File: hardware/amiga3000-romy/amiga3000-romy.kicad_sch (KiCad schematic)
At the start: 5 parts, among them IC1 GAL22V10, IC2 FAT_GARY

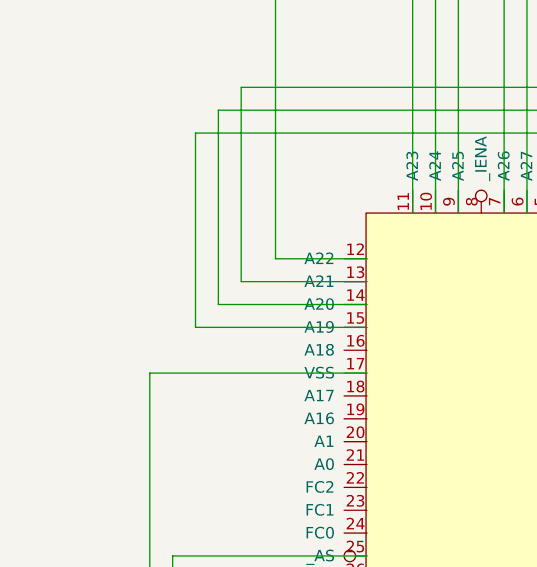
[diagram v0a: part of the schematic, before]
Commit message: Update Amiga3000 ROMY to Rev4a
major difference is the address header to support 4MB ROMs
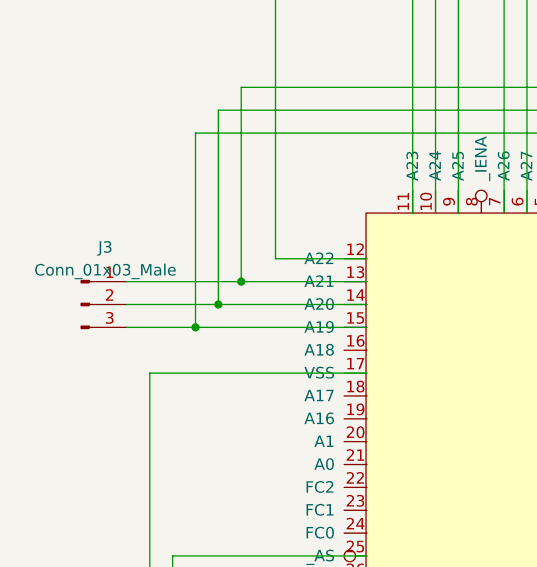
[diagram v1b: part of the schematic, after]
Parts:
- added J3: Conn_01x03_Male, Connector_PinHeader_2.54mm:PinHeader_1x03_P2.54mm_Horizontal, symbol Connector:Conn_01x03_Male
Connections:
- net at IC1.25 (IO3), IC2.13 (A21): now also J3.1 (Pin_1)
- net at IC1.24 (IO4), IC2.14 (A20): now also J3.2 (Pin_2)
- net at IC1.23 (IO5), IC2.15 (A19): now also J3.3 (Pin_3)
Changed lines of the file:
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@@
-(kicad_sch (version 20210126) (generator eeschema)
+(kicad_sch (version 20210406) (generator eeschema)
   (paper "A4")
   (title_block
@@
     (comment 4 "Re-implementation of A4k ROMY")
   )
+  (junction (at 41.91 88.9) (diameter 0.9144) (color 0 0 0 0))
+  (junction (at 44.45 86.36) (diameter 0.9144) (color 0 0 0 0))
+  (junction (at 46.99 83.82) (diameter 0.9144) (color 0 0 0 0))
   (junction (at 68.58 148.59) (diameter 0.9144) (color 0 0 0 0))
   (junction (at 68.58 165.1) (diameter 0.9144) (color 0 0 0 0))
@@
   (junction (at 154.94 92.71) (diameter 0.9144) (color 0 0 0 0))
   (junction (at 170.18 69.85) (diameter 0.9144) (color 0 0 0 0))
+  (wire (pts (xy 34.29 83.82) (xy 46.99 83.82))
+    (stroke (width 0) (type solid) (color 0 0 0 0))
+  )
+  (wire (pts (xy 34.29 86.36) (xy 44.45 86.36))
+    (stroke (width 0) (type solid) (color 0 0 0 0))
+  )
+  (wire (pts (xy 34.29 88.9) (xy 41.91 88.9))
+    (stroke (width 0) (type solid) (color 0 0 0 0))
+  )
   (wire (pts (xy 36.83 93.98) (xy 60.96 93.98))
     (stroke (width 0) (type solid) (color 0 0 0 0))
@@
   (text "~STERM\n" (at 189.23 124.46 0)
     (effects (font (size 1.27 1.27)) (justify left bottom))
+  )
+  (symbol (lib_id "Connector:Conn_01x03_Male") (at 29.21 86.36 0) (unit 1)
+    (in_bom yes) (on_board yes) (fields_autoplaced)
+    (property "Reference" "J3" (id 0) (at 31.9024 80.01 0))
+    (property "Value" "Conn_01x03_Male" (id 1) (at 31.9024 82.55 0))
+    (property "Footprint" "Connector_PinHeader_2.54mm:PinHeader_1x03_P2.54mm_Horizontal" (id 2) (at 29.21 86.36 0)
+      (effects (font (size 1.27 1.27)) hide)
+    )
+    (property "Datasheet" "~" (id 3) (at 29.21 86.36 0)
+      (effects (font (size 1.27 1.27)) hide)
+    )
+    (pin "1")
+    (pin "2")
+    (pin "3")
   )
   (symbol (lib_id "Device:C") (at 154.94 83.82 0) (unit 1)
@@
       (reference "IC2") (unit 1) (value "FAT_GARY") (footprint "amiga-romy:APW9328TH")
     )
+    (path "/8ba9560d-623e-4d70-94ad-f25be51cb833"
+      (reference "J3") (unit 1) (value "Conn_01x03_Male") (footprint "Connector_PinHeader_2.54mm:PinHeader_1x03_P2.54mm_Horizontal")
+    )
     (path "/00000000-0000-0000-0000-00005f4d260b"
